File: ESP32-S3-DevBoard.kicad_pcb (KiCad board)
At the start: 4 copper layers, 32 x 57.1 mm, 28 parts, among them J1 USB_C_Receptacle_USB2.0_14P, J2 Conn_01x22_Socket, J3 Conn_01x22_Socket, SW1 SW_Push, SW2 SW_Push, U1 ESP32-S3-WROOM-1, U2 AMS1117-3.3

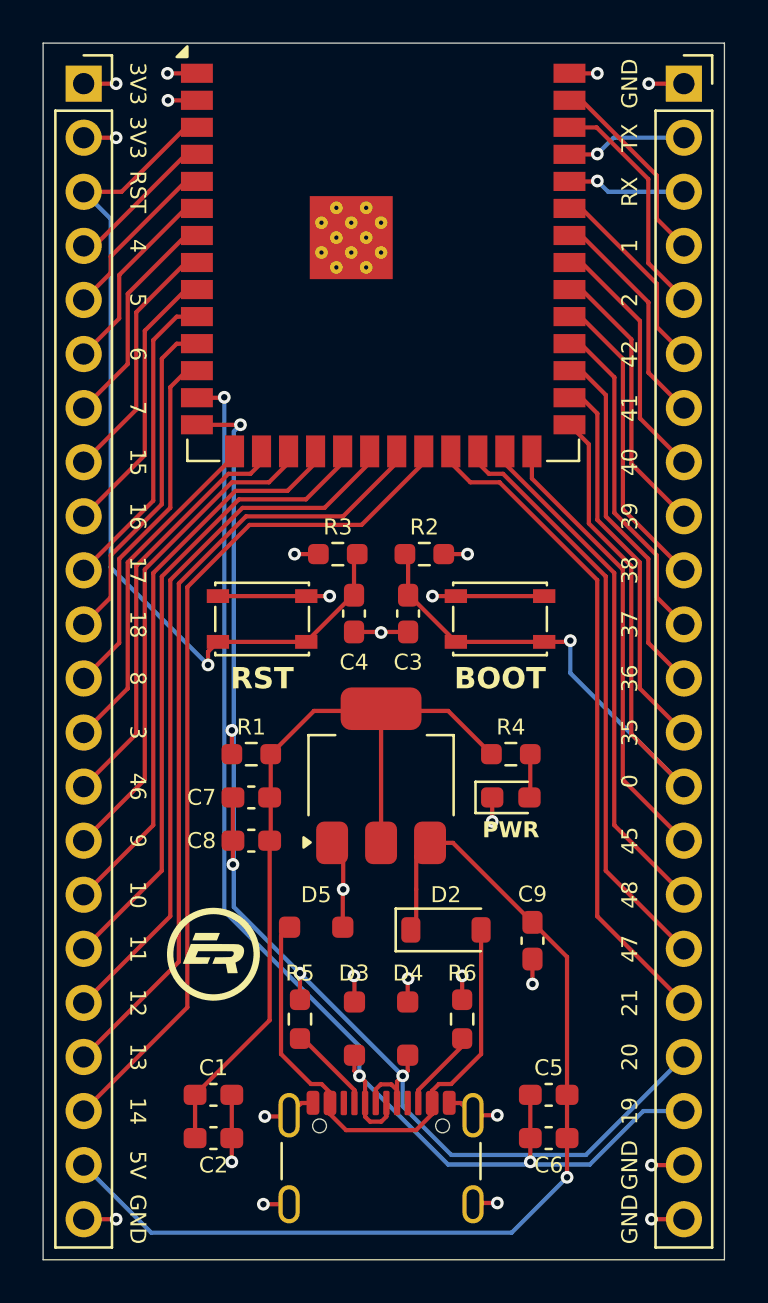
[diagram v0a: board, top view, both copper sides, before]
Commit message: Convert to through-hole vias
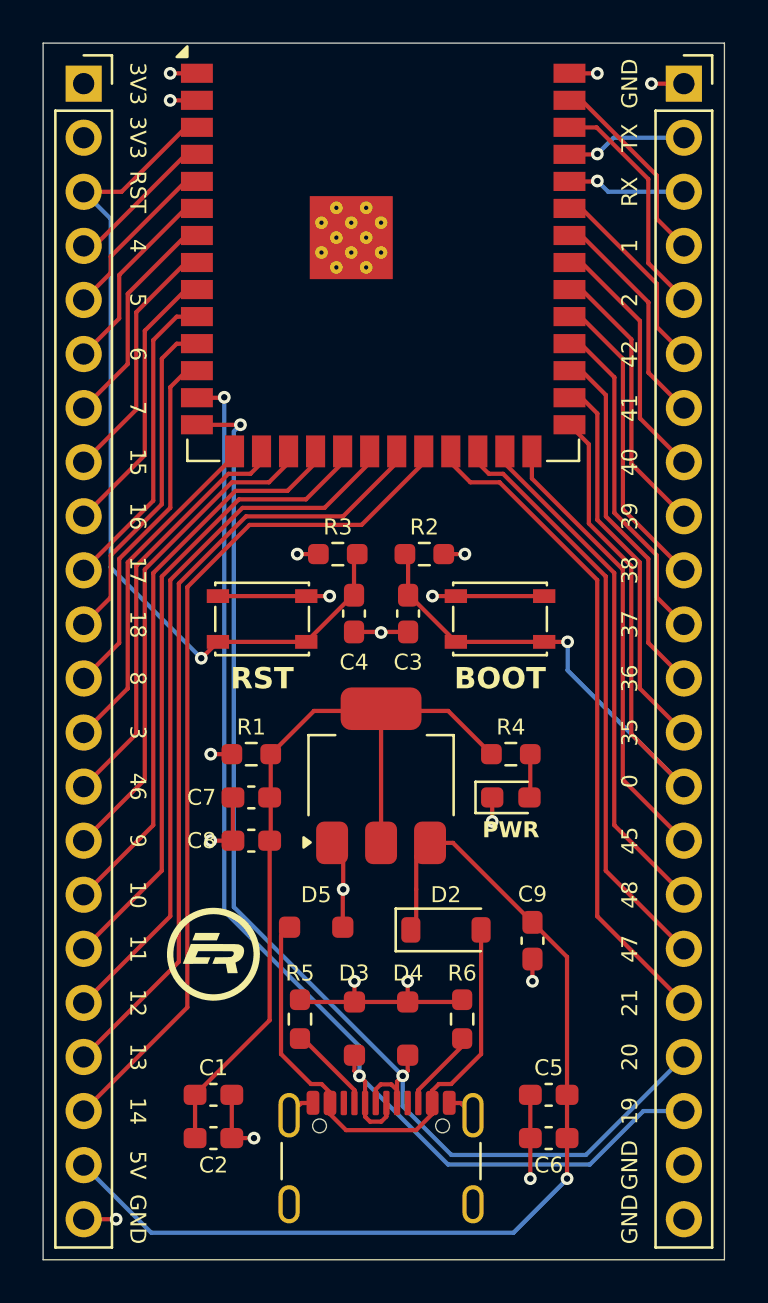
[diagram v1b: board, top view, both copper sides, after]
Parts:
- G***: footprint Footprints:ER -> Custom:ER
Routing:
- net ESP_3.3V: track 7.77 -> 4.23 mm, vias 6 -> 4
- net GND: track 51.4 -> 48.9 mm, vias 23 -> 15
- net CHIP_PU: track 41.8 -> 41.2 mm
